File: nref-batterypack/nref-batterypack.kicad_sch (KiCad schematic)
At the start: 65 parts, among them J1 BACK_CONN, J2 C4+, J3 C3-, J4 C2+, J5 C1-, J6 C1-, J7 PACK_CONN, Q1 BC817, Q2 BC817, Q3 BC817, Q4 BC817, Q5 AO3401A, Q6 DMT2005UDV, Q7 AO3401A, SW1 Reset, U1 BQ76922

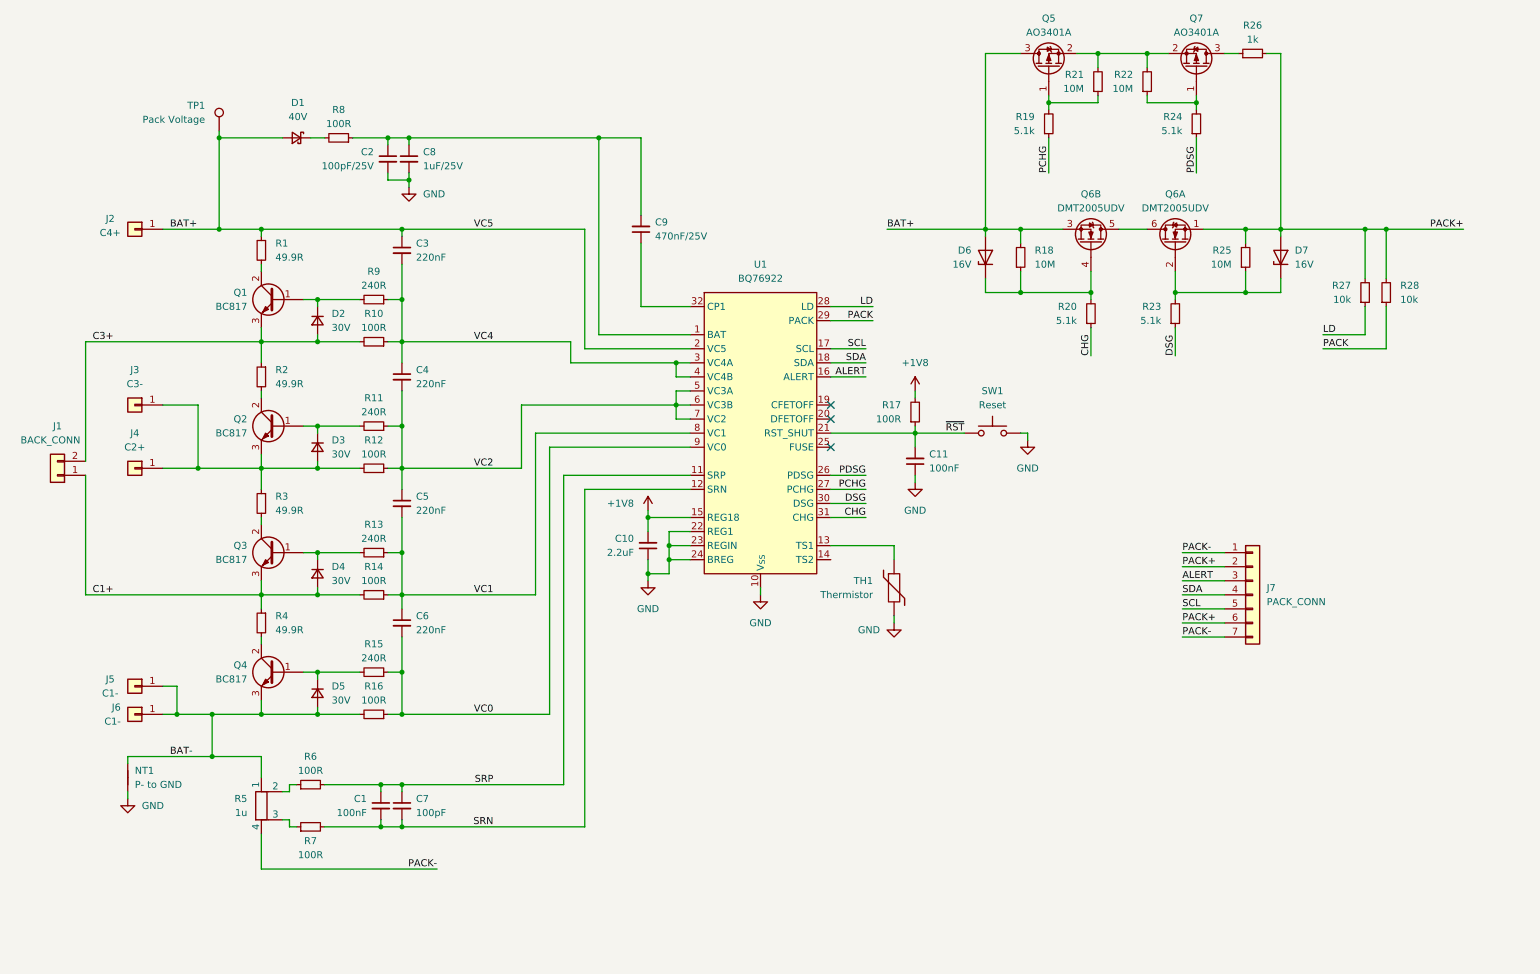
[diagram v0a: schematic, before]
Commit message: added reverse polarity indicator LEDs
+ silk on the back to indicate cell polarity
+ updated resistor values for balancing
* better b2b chg, dsg fets
+ more testpoints
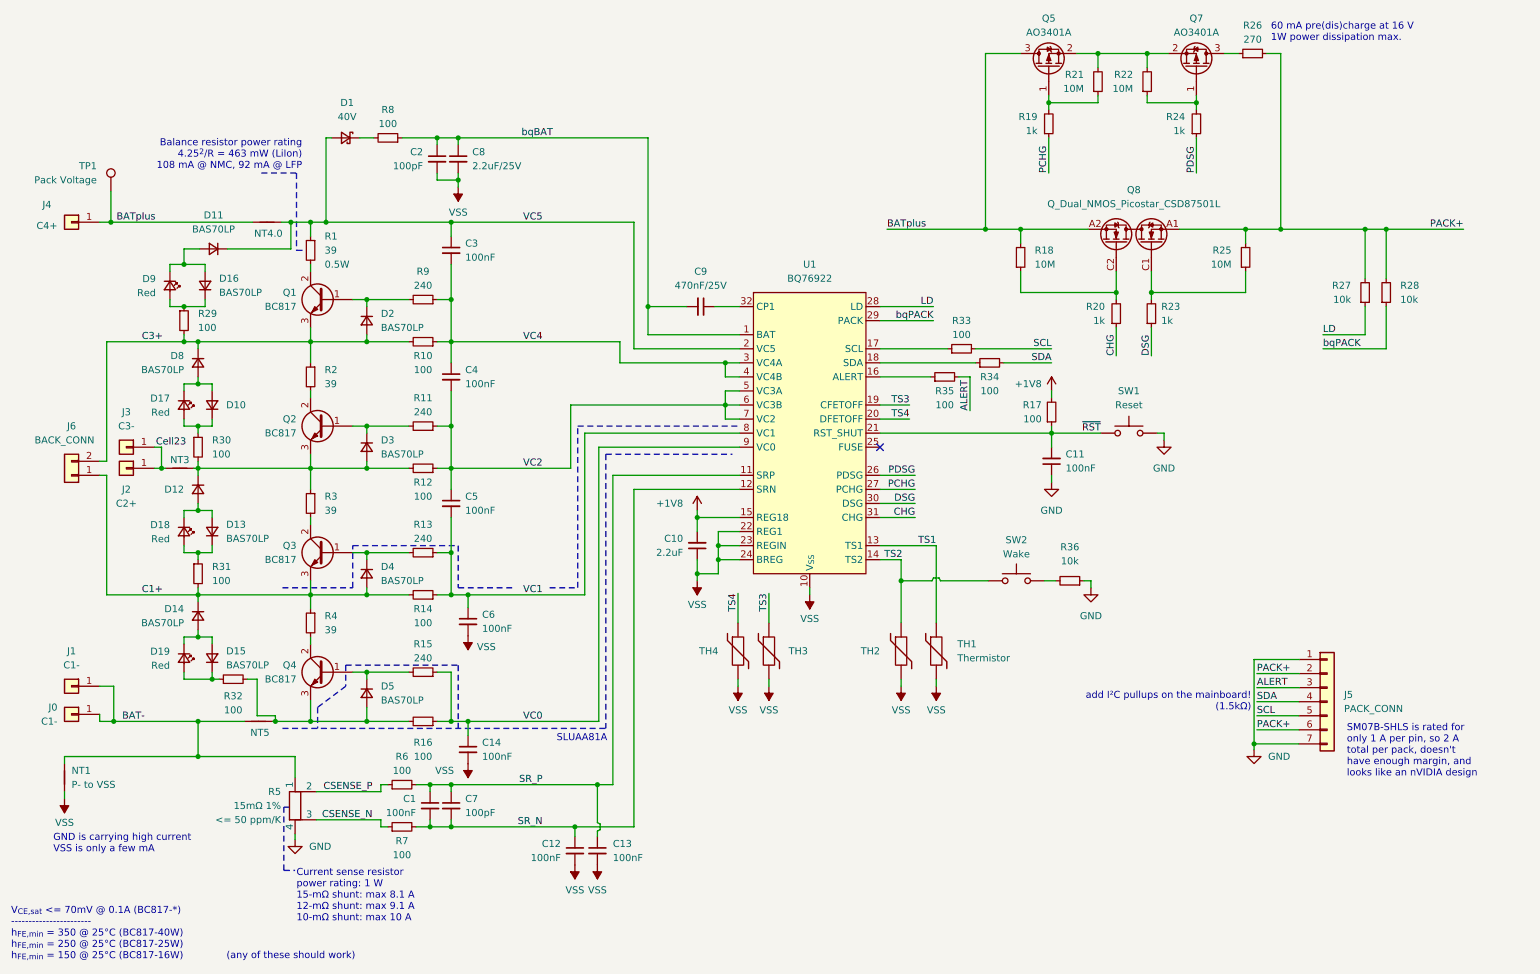
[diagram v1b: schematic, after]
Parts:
- removed D6, D7: 16V, Diode_SMD:D_SOD-323, symbol Device:D_Zener
- removed Q6: DMT2005UDV, Automated:Diodes_PowerDI3333-8_UXC_3.3x3.3mm_P0.65mm, symbol Device:Q_Dual_NMOS_S1G1S2G2D2D1
- added C12, C13, C14: 100nF, Capacitor_SMD:C_0402_1005Metric, symbol Device:C_Small
- added D10, D11, D12, D13, D14, D15, D16, D8: BAS70LP, Diode_SMD:D_SOD-882, symbol Device:D_Small
- added D17, D18, D19, D9: Red, LED_SMD:LED_0402_1005Metric, symbol Device:LED_Small
- added NT3, NT4.0, NT5: P- to GND, NetTie:NetTie-2_SMD_Pad0.5mm, symbol Device:NetTie_2
- added Q8: Q_Dual_NMOS_Picostar_CSD87501L, Automated:TI_PICOSTAR_LGA-10_3.37x1.47mm_P0.65mm, symbol meansOfCircuitDesign:Q_Dual_NMOS_Picostar_CSD87501L
- added R29, R30, R31, R32, R33, R34, R35: 100, Resistor_SMD:R_0402_1005Metric, symbol Device:R_Small
- added R36: 10k, Resistor_SMD:R_0402_1005Metric, symbol Device:R_Small
- added SW2: Wake, Button_Switch_SMD:SW_SPST_PTS810, symbol Switch:SW_Push
- added TH2, TH3, TH4: Thermistor, Resistor_SMD:R_0603_1608Metric, symbol Device:Thermistor
- C2: value 100pF/25V -> 100pF; footprint Capacitor_SMD:C_0603_1608Metric -> Capacitor_SMD:C_0402_1005Metric; MPN GCM1885C2A101JA16D -> GRM1555C1H101JA01D
- C3, C4, C5, C6: value 220nF -> 100nF; MPN GRT155C81E224KE01D -> GRM155R71C104KA88J
- C8: value 1uF/25V -> 2.2uF/25V; footprint Capacitor_SMD:C_0603_1608Metric -> Capacitor_SMD:C_0402_1005Metric; MPN GRT188R61H105KE13D -> GRM155C81E225ME11D
- C9: footprint Capacitor_SMD:C_0603_1608Metric -> Capacitor_SMD:C_0402_1005Metric; MPN GRM188R71E474KA12D -> GRM155R61H474KE11J
- D2, D3, D4, D5: value 30V -> BAS70LP; MPN PMEG3015EJ,115 -> BAS70LP-7B; Manufacturer Nexperia -> Diodes
- J1: renamed from J5; footprint footprints:S713145R -> Automated:S713145R
- J2: renamed from J4; footprint footprints:S713145R -> Automated:S713145R
- J3: footprint footprints:S713145R -> Automated:S713145R
- J4: renamed from J2; footprint footprints:S713145R -> Automated:S713145R
- NT1: value P- to GND -> P- to VSS; footprint Jumper:SolderJumper-2_P1.3mm_Bridged_RoundedPad1.0x1.5mm -> NetTie:NetTie-2_SMD_Pad0.5mm
- R1: value 49.9R -> 39; footprint Resistor_SMD:R_1206_3216Metric -> Resistor_SMD:R_1210_3225Metric; MPN RC1206FR-0749R9L -> CRGH1206J39R; Manufacturer Yageo -> TE Connextivity; Power (none) -> 0.5W
- R10, R12, R14, R16, R17, R6, R7, R8: value 100R -> 100
- R11, R13, R15, R9: value 240R -> 240
- R19, R20, R23, R24: value 5.1k -> 1k; MPN RC0402FR-075K1L -> CQ02WGF1001TCE; Manufacturer Yageo -> Royalohm
- R2, R3, R4: value 49.9R -> 39; footprint Resistor_SMD:R_1206_3216Metric -> Resistor_SMD:R_1210_3225Metric; MPN RC1206FR-0749R9L -> CRGH1206J39R; Manufacturer Yageo -> TE Connextivity
- R26: value 1k -> 270; footprint Resistor_SMD:R_1206_3216Metric -> Resistor_SMD:R_0612_1632Metric; MPN RC0402JR-071KL -> LTR18EZPF2700; Manufacturer Yageo -> Rohm
- R5: value 1u -> 15mΩ 1%; footprint Resistor_SMD:R_Shunt_Vishay_WSK2512_6332Metric_T1.19mm -> Automated:R_Shunt_Kelvin_Littlefuse_L4CA; MPN WSK25121L000FEA -> L4CA0612LR015FNR; Manufacturer Vishay Dale -> Littlefuse; Tempco (none) -> <= 50 ppm/K
- TP1: footprint TestPoint:TestPoint_Pad_1.5x1.5mm -> TestPoint:TestPoint_Pad_1.0x1.0mm
- U1: Manufacturer TI -> Texas Instruments
- renumbered J6 to J0, J7 to J5, J1 to J6
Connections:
- net PACK- is gone; now on net GND: J5.1 (Pin_1), J5.7 (Pin_7), R5.4
- net ALERT: now also R35.2; no longer U1.16 (ALERT)
- net BAT-: now also NT5.2; no longer D5.2 (A), Q4.3 (E), R16.2
- net C1+: now also D14.1 (K), R31.2
- net C3+: now also D8.1 (K), R29.2
- net GND: now also R36.1; no longer C10.1, C2.2, C8.2, NT1.1, TH1.2, U1.10 (V_{SS}), U1.22 (REG1), U1.23 (REGIN), U1.24 (BREG), U1.33 (EP)
- net PACK+: now also Q8.A1 (S1), Q8.B1 (S1), Q8.D1 (S1), Q8.E1 (S1)
- net SCL: now also R33.2; no longer U1.17 (SCL)
- net SDA: now also R34.2; no longer U1.18 (SDA)
- net VC0: now also C14.1; no longer C6.2
- net TS1: now reaches TH1.1, U1.13 (TS1)
- net at D3.2 (A), Q2.3 (E), R12.2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: now also D12.1 (K), NT3.1, R30.2; no longer J2.1 (Pin_1), J3.1 (Pin_1)
- net at R18.1, R20.2: now also Q8.C2 (G2)
- net bqBAT: now reaches C2.1, C8.1, C9.2, R8.1, U1.1 (BAT)
- net TS2: now reaches U1.14 (TS2)
- net TS2: now also SW2.2, TH2.1
- net TS3: now reaches U1.19 (CFETOFF)
- net TS3: now also TH3.1
- net TS4: now reaches U1.20 (DFETOFF)
- net TS4: now also TH4.1
- net CSENSE_P: now reaches R5.2, R6.1
- net CSENSE_N: now reaches R5.3, R7.1
- net at R23.2, R25.1: now also Q8.C1 (G1)
- net BAT+ renamed BATplus
- net BATplus: now also NT4.0.2, Q8.A2 (S2), Q8.B2 (S2), Q8.D2 (S2), Q8.E2 (S2); no longer C3.1, D1.2 (A), R1.1, U1.2 (VC5)
- net PACK renamed bqPACK
- net SRN renamed SR_N
- net SR_N: now also C12.1
- net SRP renamed SR_P
- net SR_P: now also C13.1
- new net: D12.2 (A), D13.2 (A), D18.1 (K)
- new net: D13.1 (K), D18.2 (A), R31.1
- new net: D5.2 (A), NT5.1, Q4.3 (E), R16.2, R32.2
- new net: R35.1, U1.16 (ALERT)
- new net: R33.1, U1.17 (SCL)
- new net: R34.1, U1.18 (SDA)
- new net: D10.2 (A), D17.1 (K), D8.2 (A)
- new net: D10.1 (K), D17.2 (A), R30.1
- new net: D14.2 (A), D15.2 (A), D19.1 (K)
- new net: D16.1 (K), D9.2 (A), R29.1
- new net: D15.1 (K), D19.2 (A), R32.1
- new net: D11.2 (A), D16.2 (A), D9.1 (K)
- new net: R36.2, SW2.1
- new net Cell23: J2.1 (Pin_1), J3.1 (Pin_1), NT3.2
- new net VC5: C3.1, D1.2 (A), D11.1 (K), NT4.0.1, R1.1, U1.2 (VC5)
- new net VSS: C10.1, C12.2, C13.2, C14.2, C2.2, C6.2, C8.2, NT1.1, TH1.2, TH2.2, TH3.2, TH4.2, U1.10 (V_{SS}), U1.22 (REG1), U1.23 (REGIN), U1.24 (BREG), U1.33 (EP)
- no-connect marks 3 -> 1
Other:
- note added: "(any of these should work)"
- note added: "60 mA pre(dis)charge at 16 V 1W power dissipation max."
- note added: "Balance resistor power rating 4.25^{2}/R = 463 mW (LiIon) 108 mA @ NMC, 92 mA @ LFP"
- note added: "Current sense resistor power rating: 1 W 15-mΩ shunt: max 8.1 A 12-mΩ shunt: max 9.1 A 10-mΩ shunt: max 10 A"
- note added: "GND is carrying high current VSS is only a few mA"
- note added: "SLUAA81A"
- note added: "SM07B-SHLS is rated for only 1 A per pin, so 2 A total per pack, doesn't have enough margin, and looks like an nVIDIA design"
- note added: "V_{CE,sat} <= 70mV @ 0.1A (BC817-*) ----------------------- h_{FE,min} = 350 @ 25°C (BC817-40W) h_{FE,min} = 250 @ 25°C (BC817-25W) h_{FE,min} = 150 @ 25°C (BC817-16W)"
- note added: "add I²C pullups on the mainboard! (1.5kΩ)"
- moved on the sheet: C1, C10, C11, C2, C3, C4, C5, C6, C7, C8, C9, D1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
